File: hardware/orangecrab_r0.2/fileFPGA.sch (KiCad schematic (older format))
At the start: 11 parts, among them J6 JTAG, U3 ECP5U25, U6 AT25SF081

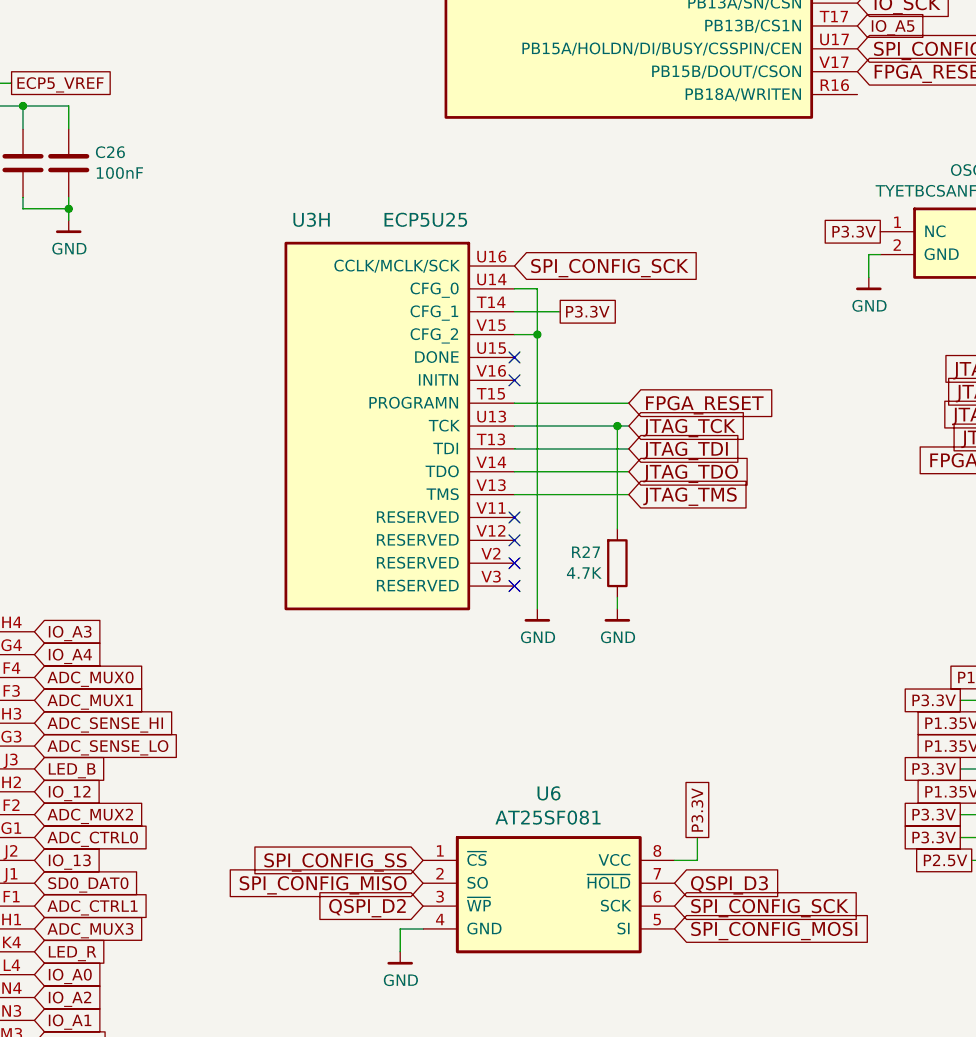
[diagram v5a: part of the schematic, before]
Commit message: hw: Update fiducials Add pullup to FLASH CS/SCK line Update BOM part numbers Fix Button pull-up voltage
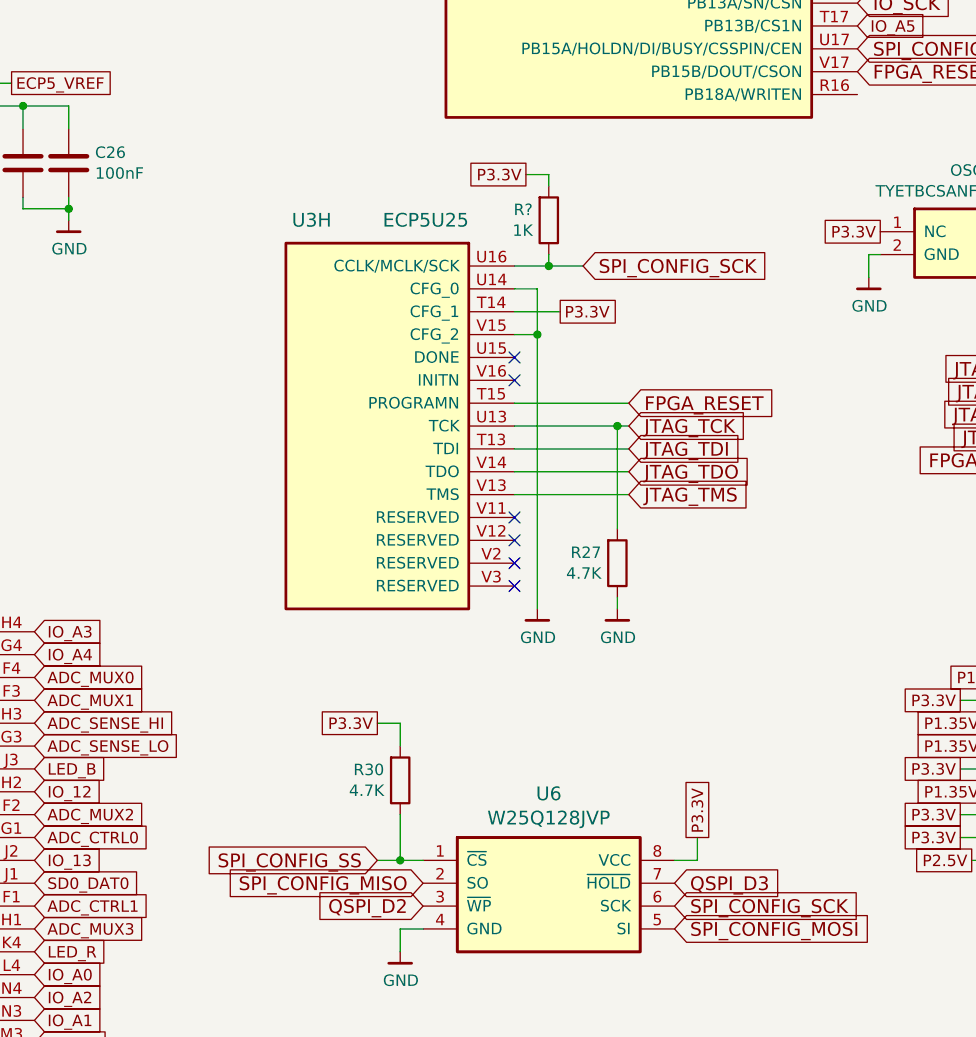
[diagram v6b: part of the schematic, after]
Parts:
- added R30: 4.7K, Resistor_SMD:R_0201_0603Metric, symbol Device:R
- added R?: 1K, Resistor_SMD:R_0201_0603Metric, symbol Device:R
- U6: value AT25SF081 -> W25Q128JVP; Mfg Adesto Technologies -> Winbond Electronics-; PN AT25SF081-MAHD-T -> W25Q128JVPIQ TR; SN-DK 1265-1275-1-ND -> (none)
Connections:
- net P3.3V: now also R30.2, R?.2
- net SPI_CONFIG_SCK: now also R?.1
- net SPI_CONFIG_SS: now also R30.1
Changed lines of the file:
@@
 Text GLabel 9300 2150 2    60   Input ~ 0
 SPI_CONFIG_SS
-Text GLabel 7800 3100 2    60   Input ~ 0
+Text GLabel 8100 3100 2    60   Input ~ 0
 SPI_CONFIG_SCK
 Text GLabel 9300 1750 2    60   Input ~ 0
@@
 AR Path="/5AB8ACB7/5D5D6375" Ref="U6"  Part="1"
 F 0 "U6" H 7950 6291 60  0000 C CNN
-F 1 "AT25SF081" H 7950 6185 60  0000 C CNN
+F 1 "W25Q128JVP" H 7950 6185 60  0000 C CNN
 F 2 "Package_SON:WSON-8-1EP_6x5mm_P1.27mm_EP3.4x4mm" H 7950 6300 60  0001 C CNN
 F 3 "" H 7950 6300 60  0001 C CNN
-F 4 "1265-1275-1-ND" H 3800 1900 50  0001 C CNN "SN-DK"
-F 5 "AT25SF081-MAHD-T" H 3800 1900 50  0001 C CNN "PN"
-F 6 "Adesto Technologies" H 7950 5850 50  0001 C CNN "Mfg"
+F 4 "" H 3800 1900 50  0001 C CNN "SN-DK"
+F 5 "W25Q128JVPIQ TR" H 3800 1900 50  0001 C CNN "PN"
+F 6 "Winbond Electronics-" H 7950 5850 50  0001 C CNN "Mfg"
 	1    7950 5850
 	1    0    0    -1
@@
 	1    0    0    -1
 $EndComp
-Text GLabel 7400 5700 0    60   Input ~ 0
+Text GLabel 7200 5700 0    60   Input ~ 0
 SPI_CONFIG_SS
 Text GLabel 8500 5900 2    60   Input ~ 0
@@
 Text GLabel 5700 4800 2    50   Input ~ 0
 IO_A4
+Wire Wire Line
+	7400 5700 7300 5700
+Wire Wire Line
+	7300 5700 7300 5500
+Connection ~ 7300 5700
+Wire Wire Line
+	7300 5700 7200 5700
+$Comp
+L Device:R R?
+U 1 1 5EA37E63
+P 7300 5350
+AR Path="/5ABC9A87/5EA37E63" Ref="R?"  Part="1"
+AR Path="/5AB8ACB7/5EA37E63" Ref="R30"  Part="1"
+F 0 "R30" H 7230 5304 50  0000 R CNN
+F 1 "4.7K" H 7230 5395 50  0000 R CNN
+F 2 "Resistor_SMD:R_0201_0603Metric" V 7230 5350 50  0001 C CNN
+F 3 "~" H 7300 5350 50  0001 C CNN
+F 4 "‎Yageo‎" H 7300 5350 50  0001 C CNN "Mfg"
+F 5 "RC0201FR-074K7L" H 7300 5350 50  0001 C CNN "PN"
+	1    7300 5350
+	1    0    0    1
+$EndComp
+Text GLabel 7200 5100 0    50   UnSpc ~ 0
+P3.3V
+Wire Wire Line
+	7200 5100 7300 5100
+Wire Wire Line
+	7300 5100 7300 5200
+Wire Wire Line
+	8100 3100 7950 3100
+$Comp
+L Device:R R?
+U 1 1 5EA70E98
+P 7950 2900
+AR Path="/5ABC9A87/5EA70E98" Ref="R?"  Part="1"
+AR Path="/5AB8ACB7/5EA70E98" Ref="R?"  Part="1"
+F 0 "R?" H 7880 2854 50  0000 R CNN
+F 1 "1K" H 7880 2945 50  0000 R CNN
+F 2 "Resistor_SMD:R_0201_0603Metric" V 7880 2900 50  0001 C CNN
+F 3 "~" H 7950 2900 50  0001 C CNN
+F 4 "‎Yageo‎" H 7950 2900 50  0001 C CNN "Mfg"
+F 5 "RC0201FR-071KL" H 7950 2900 50  0001 C CNN "PN"
+	1    7950 2900
+	1    0    0    1
+$EndComp
+Wire Wire Line
+	7950 3050 7950 3100
+Connection ~ 7950 3100
+Wire Wire Line
+	7950 3100 7800 3100
+Wire Wire Line
+	7950 2750 7950 2700
+Wire Wire Line
+	7950 2700 7850 2700
+Text GLabel 7850 2700 0    50   UnSpc ~ 0
+P3.3V
 $EndSCHEMATC

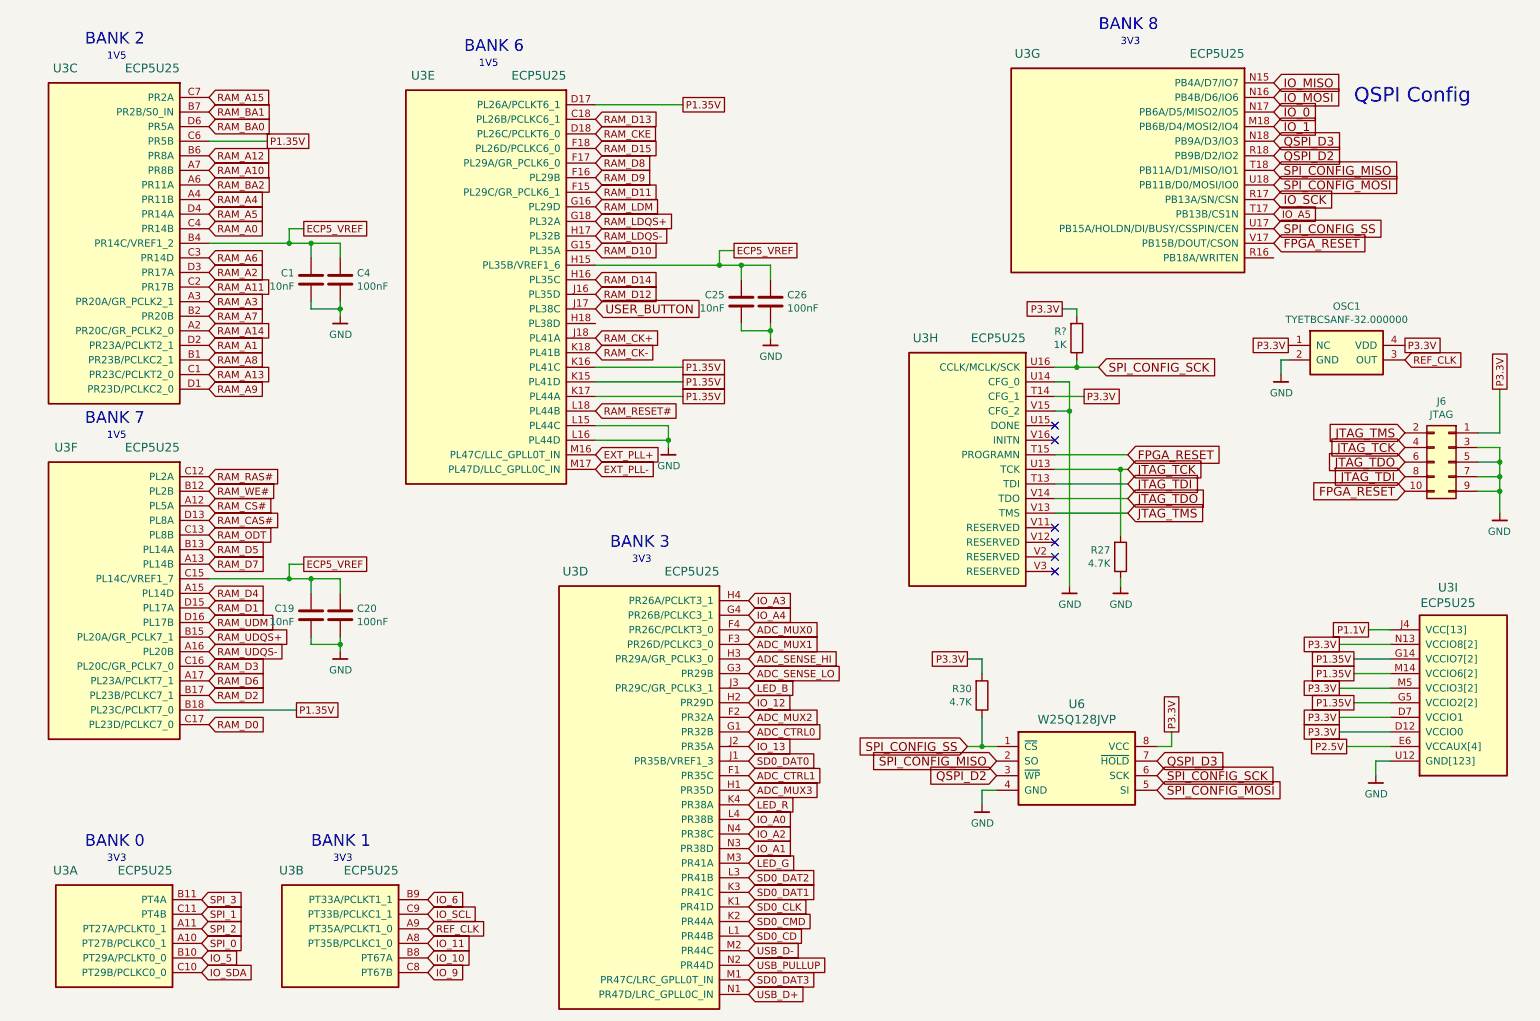
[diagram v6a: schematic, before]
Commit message: hardware/orangecrab_r0.2: r0.2 Release
Prepared KiCad files for release
Create production folder
Add pdf schematic
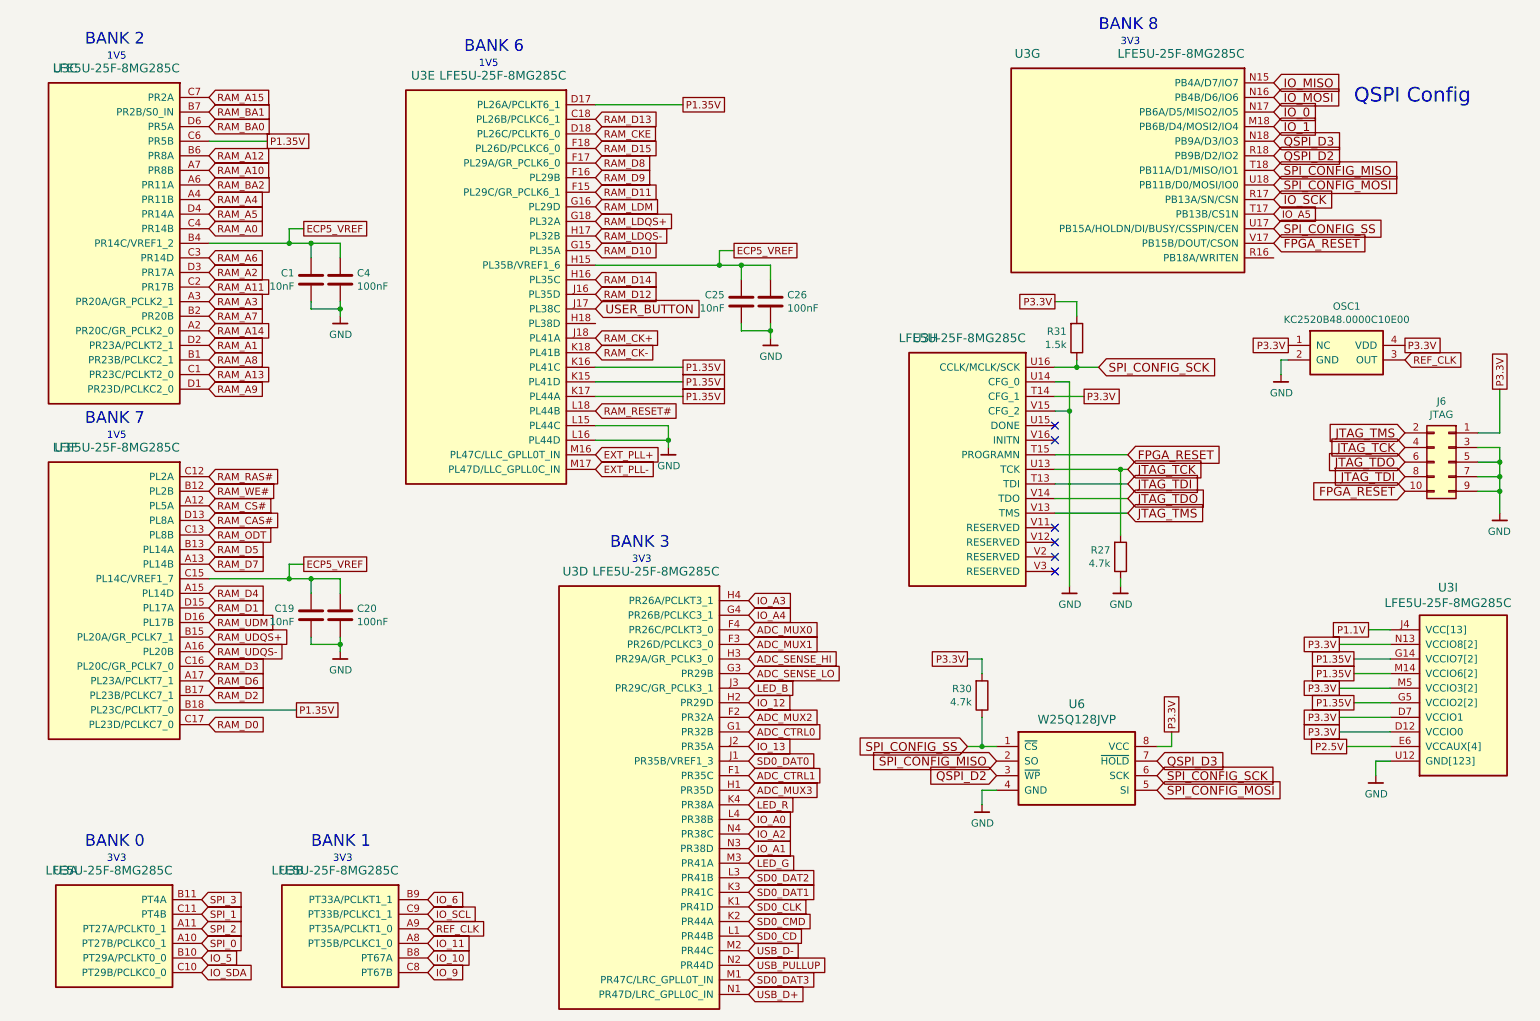
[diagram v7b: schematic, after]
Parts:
- removed R?: 1K, Resistor_SMD:R_0201_0603Metric, symbol Device:R
- added R31: 1.5k, Resistor_SMD:R_0201_0603Metric, symbol Device:R
- OSC1: value TYETBCSANF-32.000000 -> KC2520B48.0000C10E00
- R27, R30: value 4.7K -> 4.7k
- U3: value ECP5U25 -> LFE5U-25F-8MG285C
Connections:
- net P3.3V: now also R31.2
- net SPI_CONFIG_SCK: now also R31.1
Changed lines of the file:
@@
 EESchema Schematic File Version 4
-LIBS:OrangeCrab-cache
 EELAYER 30 0
 EELAYER END
@@
 Sheet 2 7
 Title "Orange Crab"
-Date "2019-06-28"
-Rev "r0.1"
-Comp "GsD"
+Date "2019-12-08"
+Rev "r0.2"
+Comp "Good Stuff Department"
 Comment1 ""
 Comment2 ""
-Comment3 ""
-Comment4 ""
+Comment3 "Licensed under CERN OHL v.1.2"
+Comment4 "Designed by: Greg Davill"
 $EndDescr
 Text GLabel 9300 2150 2    60   Input ~ 0
@@
 P 1950 6750
 F 0 "U3" H 2800 6950 60  0000 L CNN
-F 1 "ECP5U25" H 2150 6950 60  0000 L CNN
+F 1 "LFE5U-25F-8MG285C" H 2150 6950 60  0000 L CNN
 F 2 "gkl_housings_bga:csBGA285" H 1950 6750 50  0001 C CNN
 F 3 "" H 1950 6750 50  0001 C CNN
@@
 P 3500 6750
 F 0 "U3" H 4350 6950 60  0000 L CNN
-F 1 "ECP5U25" H 3700 6950 60  0000 L CNN
+F 1 "LFE5U-25F-8MG285C" H 3700 6950 60  0000 L CNN
 F 2 "gkl_housings_bga:csBGA285" H 3500 6750 50  0001 C CNN
 F 3 "" H 3500 6750 50  0001 C CNN
@@
 P 2000 1250
 F 0 "U3" H 2900 1450 60  0000 L CNN
-F 1 "ECP5U25" H 2200 1450 60  0000 L CNN
+F 1 "LFE5U-25F-8MG285C" H 2200 1450 60  0000 L CNN
 F 2 "gkl_housings_bga:csBGA285" H 2000 1250 50  0001 C CNN
 F 3 "" H 2000 1250 50  0001 C CNN
@@
 P 5700 4700
 F 0 "U3" H 6800 4900 60  0000 L CNN
-F 1 "ECP5U25" H 5900 4900 60  0000 L CNN
+F 1 "LFE5U-25F-8MG285C" H 5900 4900 60  0000 L CNN
 F 2 "gkl_housings_bga:csBGA285" H 5700 4700 50  0001 C CNN
 F 3 "" H 5700 4700 50  0001 C CNN
@@
 P 2000 3850
 F 0 "U3" H 2900 4050 60  0000 L CNN
-F 1 "ECP5U25" H 2200 4050 60  0000 L CNN
+F 1 "LFE5U-25F-8MG285C" H 2200 4050 60  0000 L CNN
 F 2 "gkl_housings_bga:csBGA285" H 2000 3850 50  0001 C CNN
 F 3 "" H 2000 3850 50  0001 C CNN
@@
 P 9300 1150
 F 0 "U3" H 10900 1350 60  0000 L CNN
-F 1 "ECP5U25" H 9500 1350 60  0000 L CNN
+F 1 "LFE5U-25F-8MG285C" H 9500 1350 60  0000 L CNN
 F 2 "gkl_housings_bga:csBGA285" H 9300 1150 50  0001 C CNN
 F 3 "" H 9300 1150 50  0001 C CNN
@@
 P 7800 3100
 F 0 "U3" H 8600 3300 60  0000 L CNN
-F 1 "ECP5U25" H 8000 3300 60  0000 L CNN
+F 1 "LFE5U-25F-8MG285C" H 8000 3300 60  0000 L CNN
 F 2 "gkl_housings_bga:csBGA285" H 7800 3100 50  0001 C CNN
 F 3 "" H 7800 3100 50  0001 C CNN
@@
 P 10100 5800
 F 0 "U3" H 10495 4610 60  0000 C CNN
-F 1 "ECP5U25" H 10495 4716 60  0000 C CNN
+F 1 "LFE5U-25F-8MG285C" H 10495 4716 60  0000 C CNN
 F 2 "gkl_housings_bga:csBGA285" H 10100 5800 50  0001 C CNN
 F 3 "" H 10100 5800 50  0001 C CNN
@@
 P 4650 1300
 F 0 "U3" H 5750 1500 60  0000 L CNN
-F 1 "ECP5U25" H 4850 1500 60  0000 L CNN
+F 1 "LFE5U-25F-8MG285C" H 4850 1500 60  0000 L CNN
 F 2 "gkl_housings_bga:csBGA285" H 4650 1300 50  0001 C CNN
 F 3 "" H 4650 1300 50  0001 C CNN
@@
 P 9800 3000
 F 0 "OSC1" H 9800 3318 50  0000 C CNN
-F 1 "TYETBCSANF-32.000000" H 9800 3227 50  0000 C CNN
+F 1 "KC2520B48.0000C10E00" H 9800 3227 50  0000 C CNN
 F 2 "gkl_time:Oscilator_2.5x2.0" H 9800 3250 50  0001 C CNN
 F 3 "" H 9800 3250 50  0001 C CNN
@@
 AR Path="/5AB8ACB7/5D593C8A" Ref="R27"  Part="1"
 F 0 "R27" H 8180 4354 50  0000 R CNN
-F 1 "4.7K" H 8180 4445 50  0000 R CNN
+F 1 "4.7k" H 8180 4445 50  0000 R CNN
 F 2 "Resistor_SMD:R_0201_0603Metric" V 8180 4400 50  0001 C CNN
 F 3 "~" H 8250 4400 50  0001 C CNN
@@
 AR Path="/5AB8ACB7/5EA37E63" Ref="R30"  Part="1"
 F 0 "R30" H 7230 5304 50  0000 R CNN
-F 1 "4.7K" H 7230 5395 50  0000 R CNN
+F 1 "4.7k" H 7230 5395 50  0000 R CNN
 F 2 "Resistor_SMD:R_0201_0603Metric" V 7230 5350 50  0001 C CNN
 F 3 "~" H 7300 5350 50  0001 C CNN
@@
 	7300 5100 7300 5200
 Wire Wire Line
-	8100 3100 7950 3100
+	7800 3100 7950 3100
 $Comp
 L Device:R R?
-U 1 1 5EA70E98
+U 1 1 5E39317C
 P 7950 2900
-AR Path="/5ABC9A87/5EA70E98" Ref="R?"  Part="1"
-AR Path="/5AB8ACB7/5EA70E98" Ref="R?"  Part="1"
-F 0 "R?" H 7880 2854 50  0000 R CNN
-F 1 "1K" H 7880 2945 50  0000 R CNN
+AR Path="/5ABC9A87/5E39317C" Ref="R?"  Part="1"
+AR Path="/5AB8ACB7/5E39317C" Ref="R31"  Part="1"
+F 0 "R31" H 7880 2854 50  0000 R CNN
+F 1 "1.5k" H 7880 2945 50  0000 R CNN
 F 2 "Resistor_SMD:R_0201_0603Metric" V 7880 2900 50  0001 C CNN
 F 3 "~" H 7950 2900 50  0001 C CNN
 F 4 "‎Yageo‎" H 7950 2900 50  0001 C CNN "Mfg"
-F 5 "RC0201FR-071KL" H 7950 2900 50  0001 C CNN "PN"
+F 5 "RC0201FR-071K5L" H 7950 2900 50  0001 C CNN "PN"
 	1    7950 2900
 	1    0    0    1
@@
 Connection ~ 7950 3100
 Wire Wire Line
-	7950 3100 7800 3100
-Wire Wire Line
-	7950 2750 7950 2700
-Wire Wire Line
-	7950 2700 7850 2700
-Text GLabel 7850 2700 0    50   UnSpc ~ 0
+	7950 3100 8100 3100
+Wire Wire Line
+	7950 2750 7950 2650
+Wire Wire Line
+	7950 2650 7800 2650
+Text GLabel 7800 2650 0    50   UnSpc ~ 0
 P3.3V
 $EndSCHEMATC
